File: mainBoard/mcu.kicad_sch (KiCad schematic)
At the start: 36 parts, among them J2 USB_A, SW2 SW_SPDT, SW3 SW_Push, SW4 SW_Push, U19 23LC1024-I/ST, U5 USBLC6-2SC6, U6 STM32F413RHT6, Y1 ATS240C-E

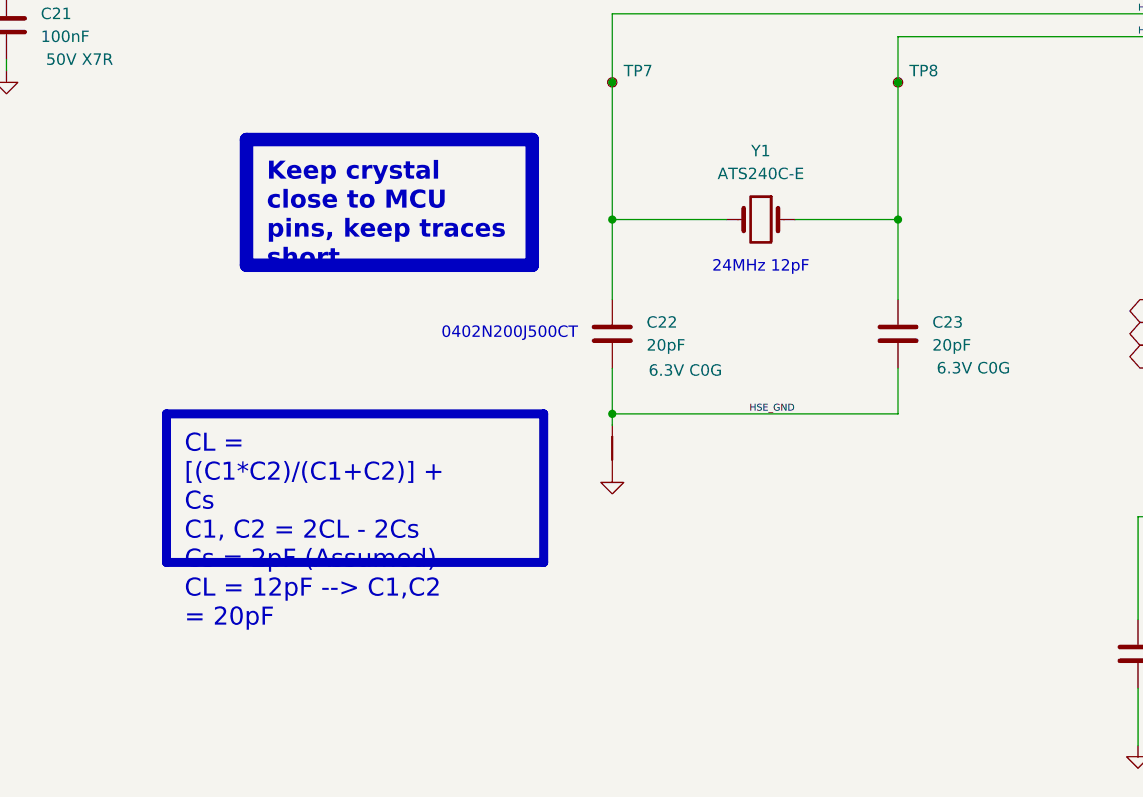
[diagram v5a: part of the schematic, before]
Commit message: change to 48MHz crystal
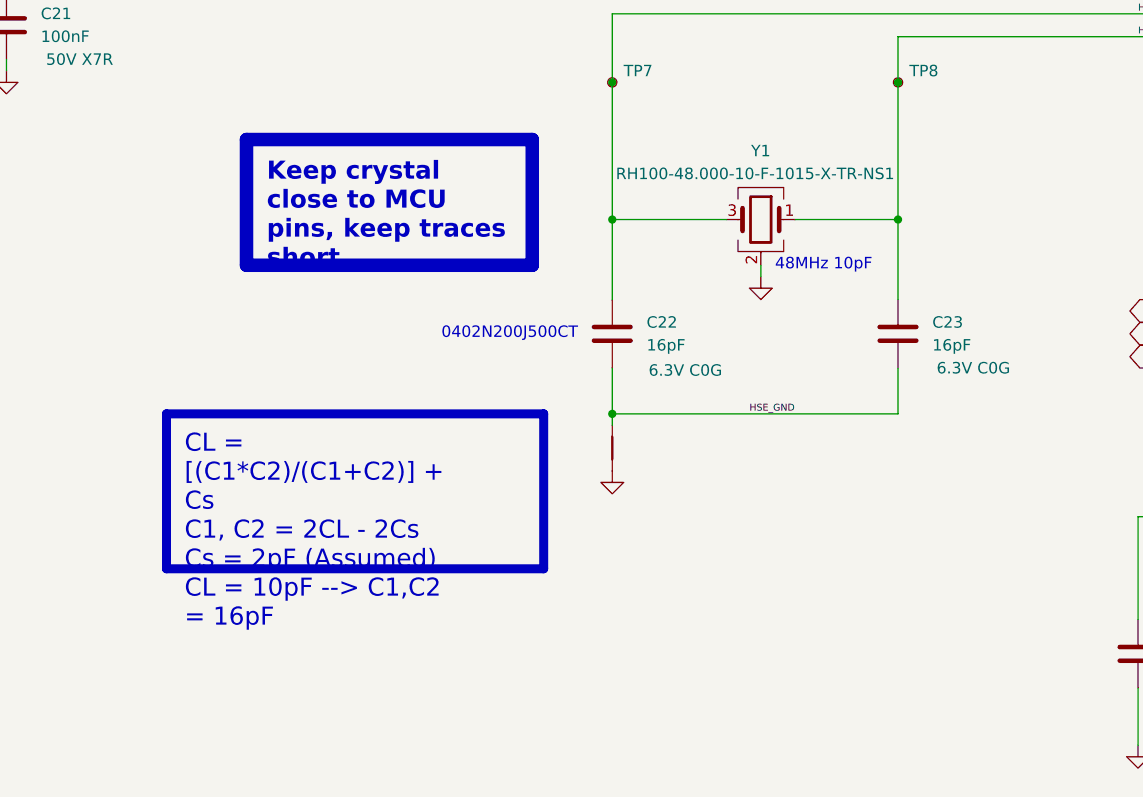
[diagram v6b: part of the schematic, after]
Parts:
- C22, C23: value 20pF -> 16pF
- Y1: value ATS240C-E -> RH100-48.000-10-F-1015-X-TR-NS1; symbol Device:Crystal -> Device:Crystal_GND24
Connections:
- net GND: now also Y1.2 (G), Y1.4 (G)
- net HSE_IN: now also Y1.3; no longer Y1.2
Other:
- note added: "48MHz 10pF"
- note removed: "24MHz 12pF"
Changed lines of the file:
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@@
 		)
 	)
-	(text "24MHz 12pF"
+	(text "48MHz 10pF"
 		(exclude_from_sim no)
-		(at 186.69 153.924 0)
+		(at 193.675 153.67 0)
 		(effects
 			(font
@@
 		)
 	)
-	(text_box "CL = [(C1*C2)/(C1+C2)] + Cs\nC1, C2 = 2CL - 2Cs\nCs = 2pF (Assumed)\nCL = 12pF --> C1,C2 = 20pF"
+	(text_box "CL = [(C1*C2)/(C1+C2)] + Cs\nC1, C2 = 2CL - 2Cs\nCs = 2pF (Assumed)\nCL = 10pF --> C1,C2 = 16pF"
 		(exclude_from_sim no)
 		(at 120.65 170.18 0)
-		(size 41.91 16.51)
+		(size 41.91 17.214)
 		(margins 2 2 2 2)
 		(stroke
@@
 	(wire
 		(pts
+			(xy 186.69 153.67) (xy 186.69 154.94)
+		)
+		(stroke
+			(width 0)
+			(type default)
+		)
+	)
+	(wire
+		(pts
 			(xy 294.64 72.39) (xy 294.64 69.85)
 		)
@@
 			)
 		)
-		(property "Value" "20pF"
+		(property "Value" "16pF"
 			(at 205.74 162.5599 0)
 			(show_name no)
@@
 	(symbol
 		(lib_id "power:GND")
+		(at 186.69 154.94 0)
+		(unit 1)
+		(body_style 1)
+		(exclude_from_sim no)
+		(in_bom yes)
+		(on_board yes)
+		(in_pos_files yes)
+		(dnp no)
+		(fields_autoplaced yes)
+		(property "Reference" "#PWR0107"
+			(at 186.69 161.29 0)
+			(hide yes)
+			(show_name no)
+			(do_not_autoplace no)
+			(effects
+				(font
+					(size 1.27 1.27)
+				)
+			)
+		)
+		(property "Value" "GND"
+			(at 186.69 160.02 0)
+			(hide yes)
+			(show_name no)
+			(do_not_autoplace no)
+			(effects
+				(font
+					(size 1.27 1.27)
+				)
+			)
+		)
+		(property "Footprint" ""
+			(at 186.69 154.94 0)
+			(hide yes)
+			(show_name no)
+			(do_not_autoplace no)
+			(effects
+				(font
+					(size 1.27 1.27)
+				)
+			)
+		)
+		(property "Datasheet" ""
+			(at 186.69 154.94 0)
+			(hide yes)
+			(show_name no)
+			(do_not_autoplace no)
+			(effects
+				(font
+					(size 1.27 1.27)
+				)
+			)
+		)
+		(property "Description" "Power symbol creates a global label with name \"GND\" , ground"
+			(at 186.69 154.94 0)
+			(hide yes)
+			(show_name no)
+			(do_not_autoplace no)
+			(effects
+				(font
+					(size 1.27 1.27)
+				)
+			)
+		)
+		(pin "1"
+		)
+		(instances
+			(project "mainBoard"
+				(path "/0650c7a8-acba-429c-9f8e-eec0baf0bc1c/fede4c36-00cc-4d3d-b71c-5243ba232202/7d5a1283-086b-46b0-8df7-a9850521fb5e"
+					(reference "#PWR0107")
+					(unit 1)
+				)
+			)
+		)
+	)
+	(symbol
+		(lib_id "power:GND")
 		(at 55.88 212.09 0)
 		(unit 1)
@@
 	)
 	(symbol
-		(lib_id "Device:Crystal")
+		(lib_id "Device:Crystal_GND24")
 		(at 186.69 148.59 0)
 		(mirror y)
@@
 			)
 		)
-		(property "Value" "ATS240C-E"
-			(at 186.69 143.51 0)
+		(property "Value" "RH100-48.000-10-F-1015-X-TR-NS1"
+			(at 186.055 143.51 0)
 			(show_name no)
 			(do_not_autoplace no)
@@
 			)
 		)
-		(property "Description" "Two pin crystal"
+		(property "Description" "Four pin crystal, GND on pins 2 and 4"
 			(at 186.69 148.59 0)
 			(hide yes)
@@
 		(pin "1"
 		)
+		(pin "4"
+		)
+		(pin "3"
+		)
 		(instances
 			(project "mainBoard"
@@
 			)
 		)
-		(property "Value" "20pF"
+		(property "Value" "16pF"
 			(at 173.99 162.5599 0)
 			(show_name no)
